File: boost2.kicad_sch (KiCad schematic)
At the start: 18 parts, among them Q2 G1003B-23, U4 LM3478MA

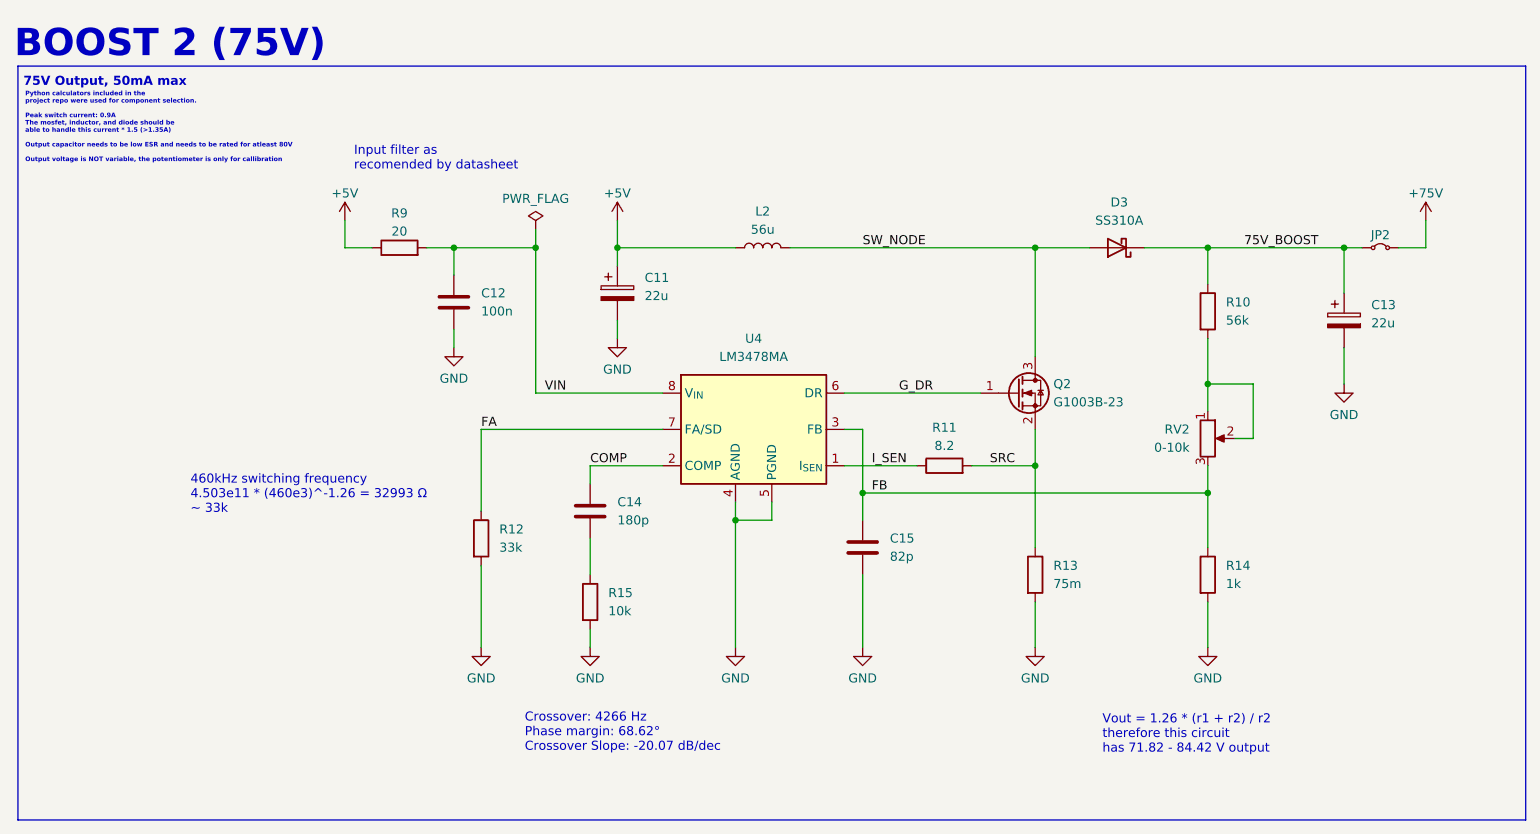
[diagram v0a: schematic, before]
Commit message: Added onboard MCU
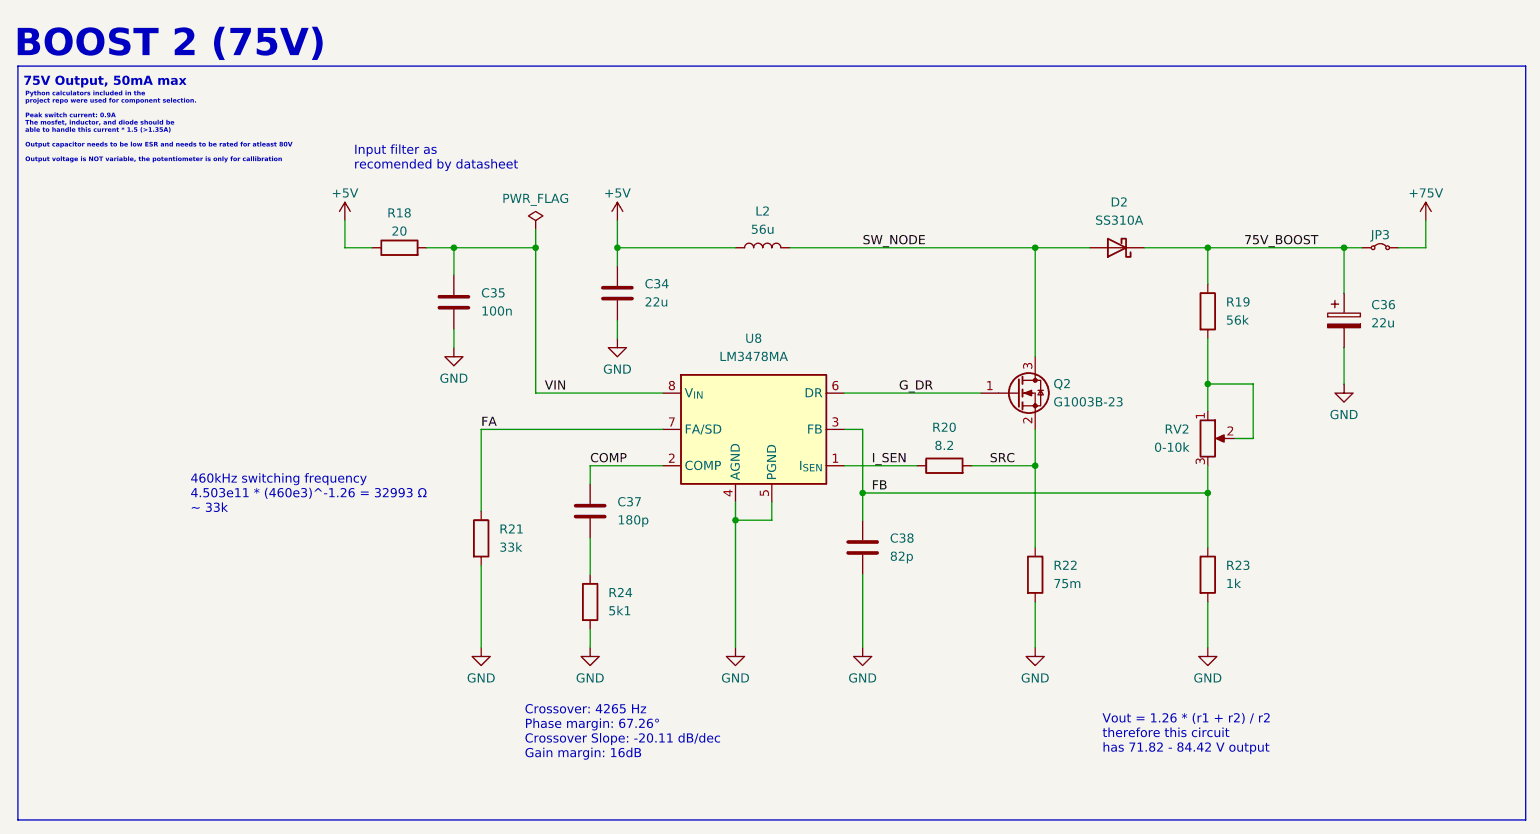
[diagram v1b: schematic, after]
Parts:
- removed C11: 22u, Capacitor_THT:CP_Radial_D6.3mm_P2.50mm, symbol Device:C_Polarized
- removed R15: 10k, Resistor_SMD:R_0603_1608Metric, symbol Device:R
- added C34: 22u, Capacitor_SMD:C_0603_1608Metric, symbol Device:C
- added R24: 5k1, Resistor_SMD:R_0603_1608Metric, symbol Device:R
- JP3: renamed from JP2; LCSC PART # C41432920 -> (none)
- renumbered C12 to C35, C13 to C36, C14 to C37, C15 to C38, D3 to D2, R9 to R18, R10 to R19, R11 to R20, R12 to R21, R13 to R22, R14 to R23, U4 to U8
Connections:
- net +5V: now also C34.1
- net GND: now also C34.2, R24.2
- net at C37.2: now also R24.1
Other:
- note added: "Crossover: 4265 Hz Phase margin: 67.26° Crossover Slope: -20.11 dB/dec Gain margin: 16dB"
- note removed: "Crossover: 4266 Hz Phase margin: 68.62° Crossover Slope: -20.07 dB/dec"
